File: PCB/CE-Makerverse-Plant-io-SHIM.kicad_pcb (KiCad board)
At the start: 2 copper layers, 42.5 x 53 mm, 43 parts, among them J1 Pump_Conn, J2 Sol_Conn, J3 Conn_PiicoDev_socket, U1 RaspberryPi_Pico_R3

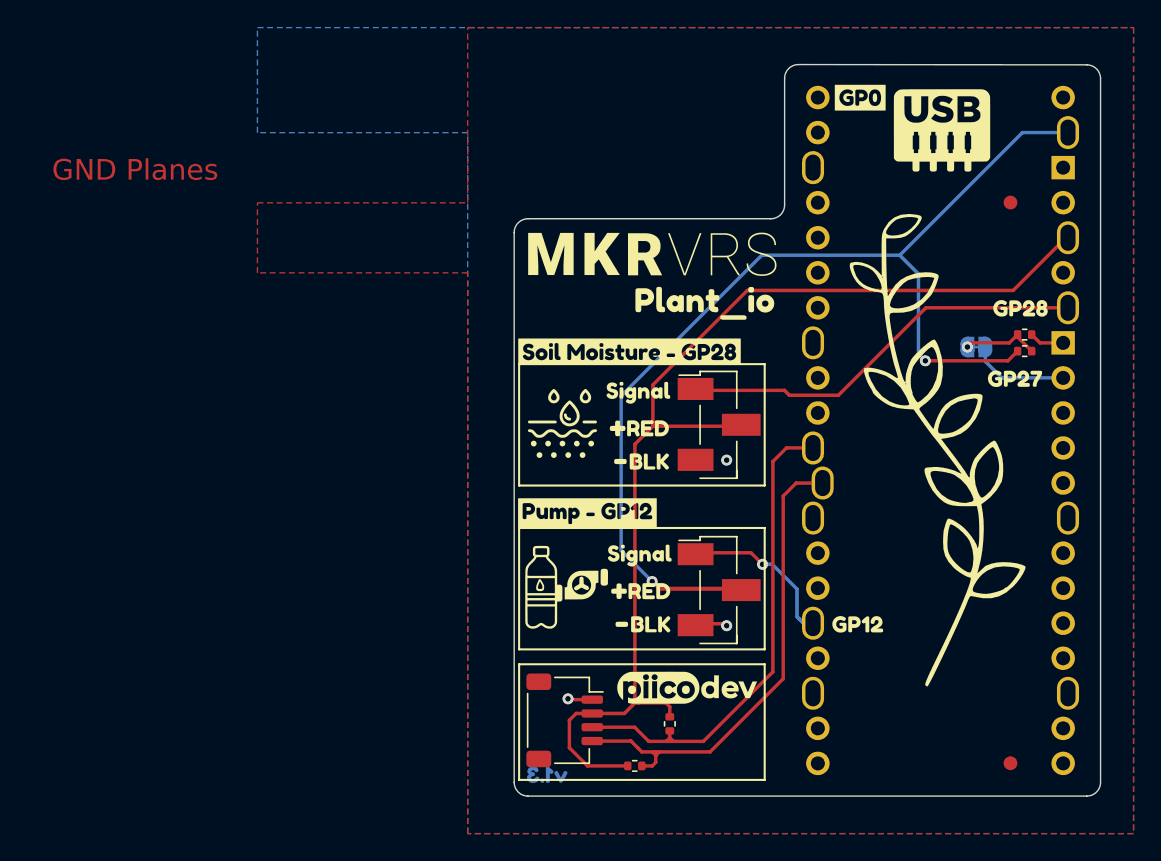
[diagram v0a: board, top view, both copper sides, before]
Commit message: v1.3 fix minor edge cut and fill
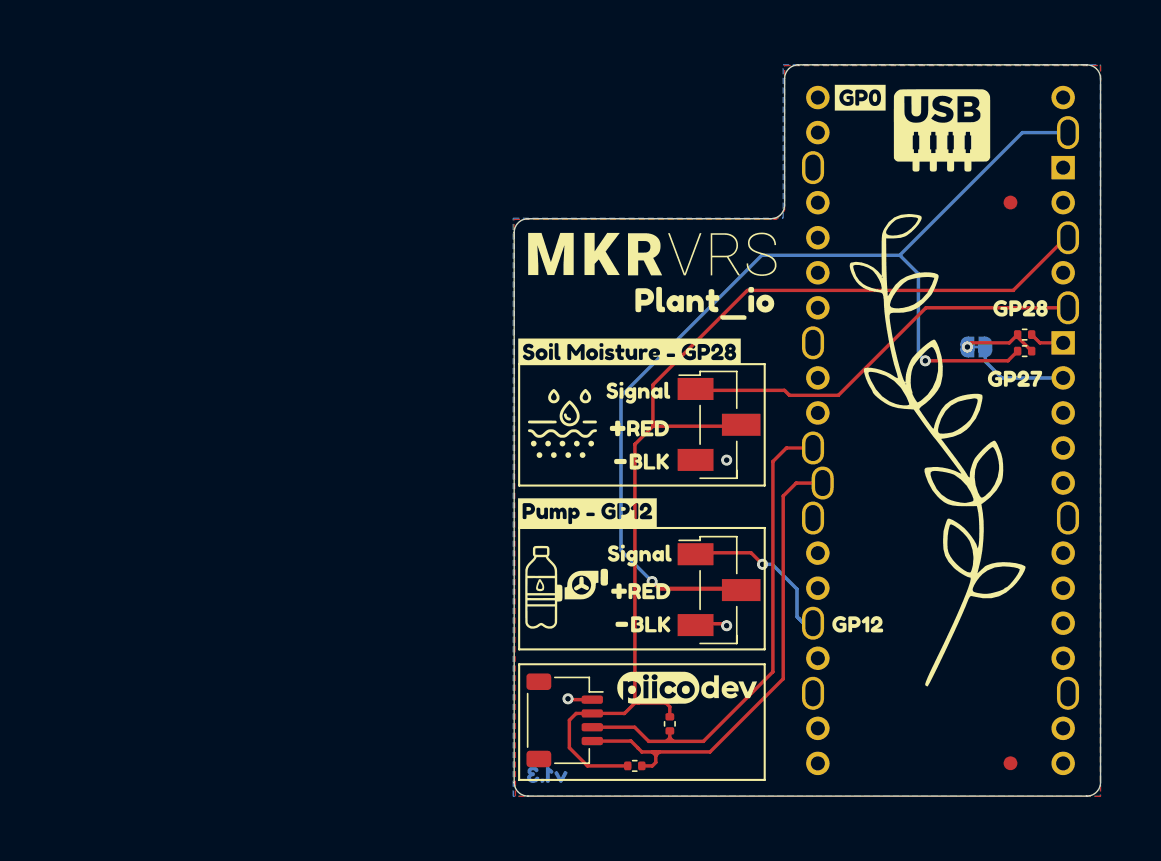
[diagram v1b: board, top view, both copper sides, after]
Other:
- board text removed: "GND Planes"
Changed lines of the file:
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@@
   (gr_rect (start 105.908 84.6176) (end 88.108 75.8176) (layer "F.SilkS") (width 0.15) (fill none))
   (gr_line (start 87.750001 54.4056) (end 87.750001 94.249999) (layer "Edge.Cuts") (width 0.1))
-  (gr_line (start 107.350001 43.2296) (end 107.350001 52.4056) (layer "Edge.Cuts") (width 0.1))
+  (gr_line (start 107.350001 43.250001) (end 107.350001 52.4056) (layer "Edge.Cuts") (width 0.1))
   (gr_line (start 129.249999 95.249999) (end 88.750001 95.249999) (layer "Edge.Cuts") (width 0.1))
-  (gr_line (start 108.350001 42.2296) (end 129.249999 42.250001) (layer "Edge.Cuts") (width 0.1))
+  (gr_line (start 108.350001 42.250001) (end 129.249999 42.250001) (layer "Edge.Cuts") (width 0.1))
   (gr_arc (start 87.750001 54.4056) (mid 88.042894 53.698493) (end 88.750001 53.4056) (layer "Edge.Cuts") (width 0.1))
   (gr_arc (start 107.350001 52.4056) (mid 107.057108 53.112707) (end 106.350001 53.4056) (layer "Edge.Cuts") (width 0.1))
@@
   (gr_line (start 130.249999 43.250001) (end 130.249999 94.249999) (layer "Edge.Cuts") (width 0.1))
   (gr_line (start 106.350001 53.4056) (end 88.750001 53.4056) (layer "Edge.Cuts") (width 0.1))
-  (gr_arc (start 107.350001 43.2296) (mid 107.642894 42.522493) (end 108.350001 42.2296) (layer "Edge.Cuts") (width 0.1))
-  (gr_text "GND Planes" (at 60.282 49.8796) (layer "F.Cu")
-    (effects (font (size 1.5 1.5) (thickness 0.3)))
-  )
+  (gr_arc (start 107.350001 43.250001) (mid 107.642894 42.542895) (end 108.350001 42.250001) (layer "Edge.Cuts") (width 0.1))
   (gr_text "Plant Cultivation\nSHIM" (at 97.55 85.3) (layer "B.SilkS")
     (effects (font (size 1.3 1.3) (thickness 0.25)) (justify mirror))
@@
     (polygon
       (pts
-        (xy 132.642 97.9696)
-        (xy 84.382 97.9696)
-        (xy 84.382 57.3296)
-        (xy 69.142 57.3296)
-        (xy 69.142 52.2496)
-        (xy 84.382 52.2496)
-        (xy 84.382 39.5496)
-        (xy 132.642 39.5496)
+        (xy 130.242 95.2696)
+        (xy 87.840336 95.269495)
+        (xy 87.740302 53.449576)
+        (xy 106.75 53.449622)
+        (xy 107.35 52.8)
+        (xy 107.35 42.3)
+        (xy 130.25 42.3)
       )
     )
@@
     (polygon
       (pts
-        (xy 132.642 97.9696)
-        (xy 84.382 97.9696)
-        (xy 84.382 47.1696)
-        (xy 69.142 47.1696)
-        (xy 69.142 39.5496)
-        (xy 132.642 39.5496)
+        (xy 130.242 95.2696)
+        (xy 87.682 95.2696)
+        (xy 87.682 53.3696)
+        (xy 107.242 53.3696)
+        (xy 107.242 42.2496)
+        (xy 130.242 42.2496)
       )
     )
